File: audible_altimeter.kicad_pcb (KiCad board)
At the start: 2 copper layers, 43 parts, among them CON1 BUQ2-USB-MICRO-B, IC1 BUQ2-ATXMEGA128A4U-A, P1 CONN_2, Q1 NPN, U1 MCP7940M, U10 LINX-FM-GPS, U11 SI7020-A10, U2 MCP73831-SOT-23-5, U3 NCP4681-SC-70, U4 MICRO-SD-CONN, U5 MPL3115A2, U6 LS013B4DN04, U7 CSS-0575A-SMT, U8 TAG-CONNECT-ATMEL-PDI-CONNECT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, U9 MPU-9250, X1 CRYSTAL

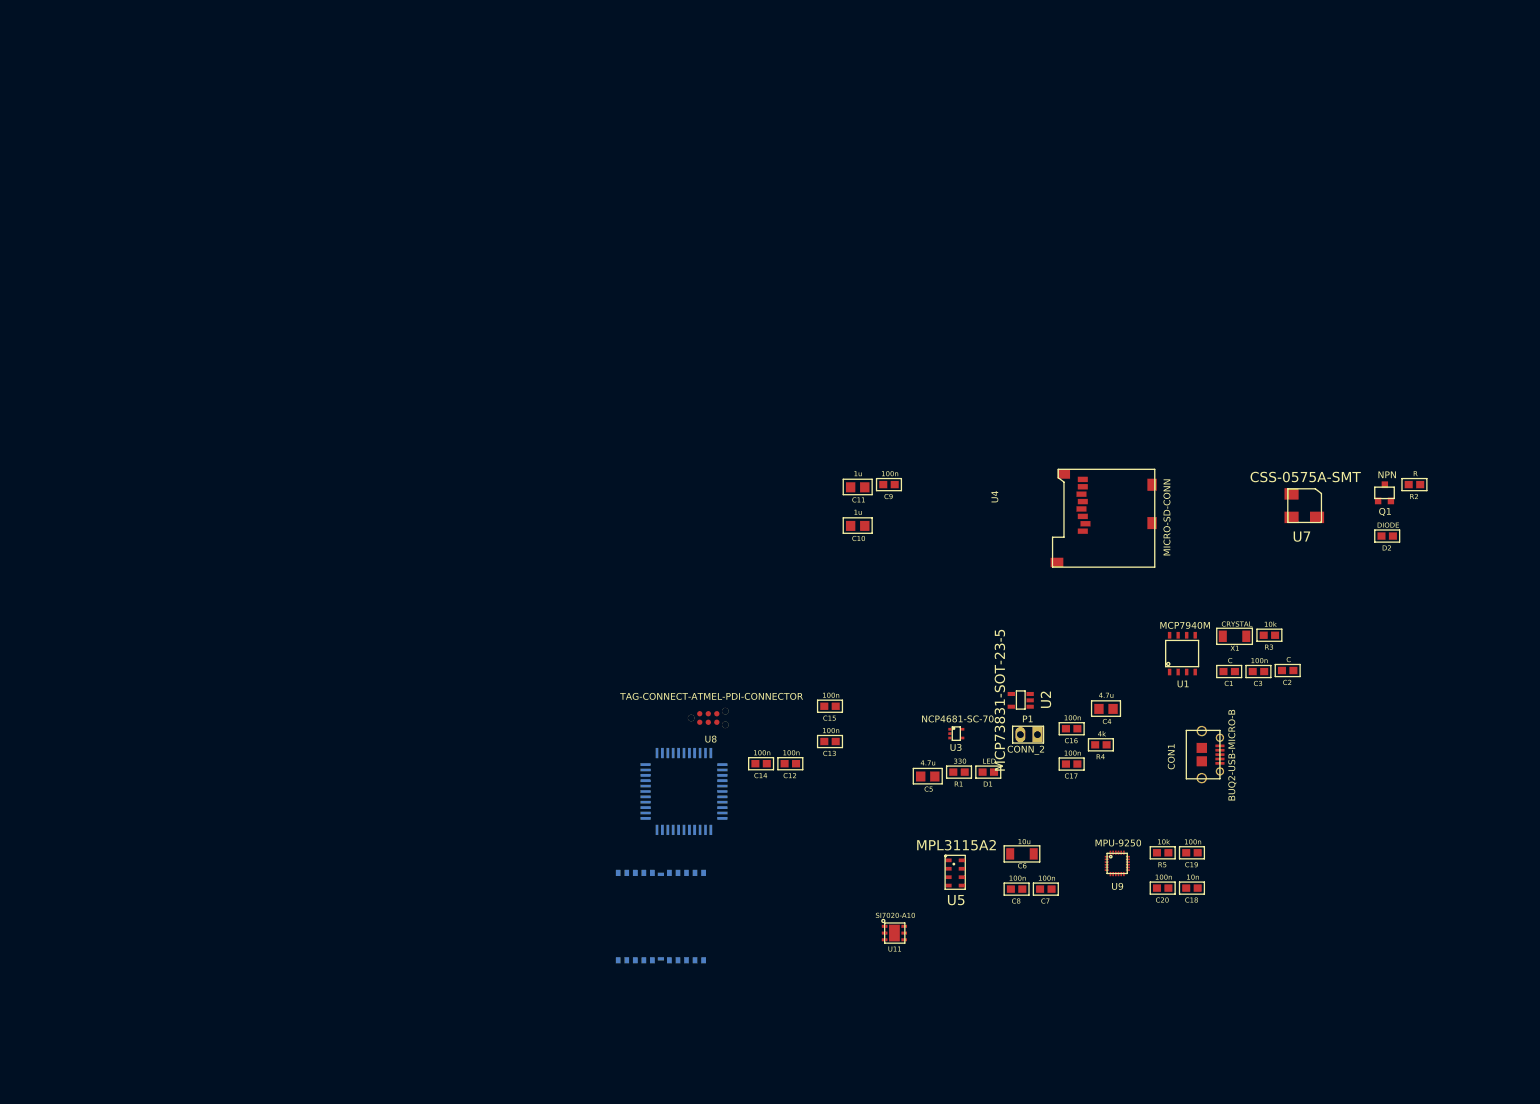
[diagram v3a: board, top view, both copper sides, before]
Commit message: Add buttons. Fix DRC. Add antenna
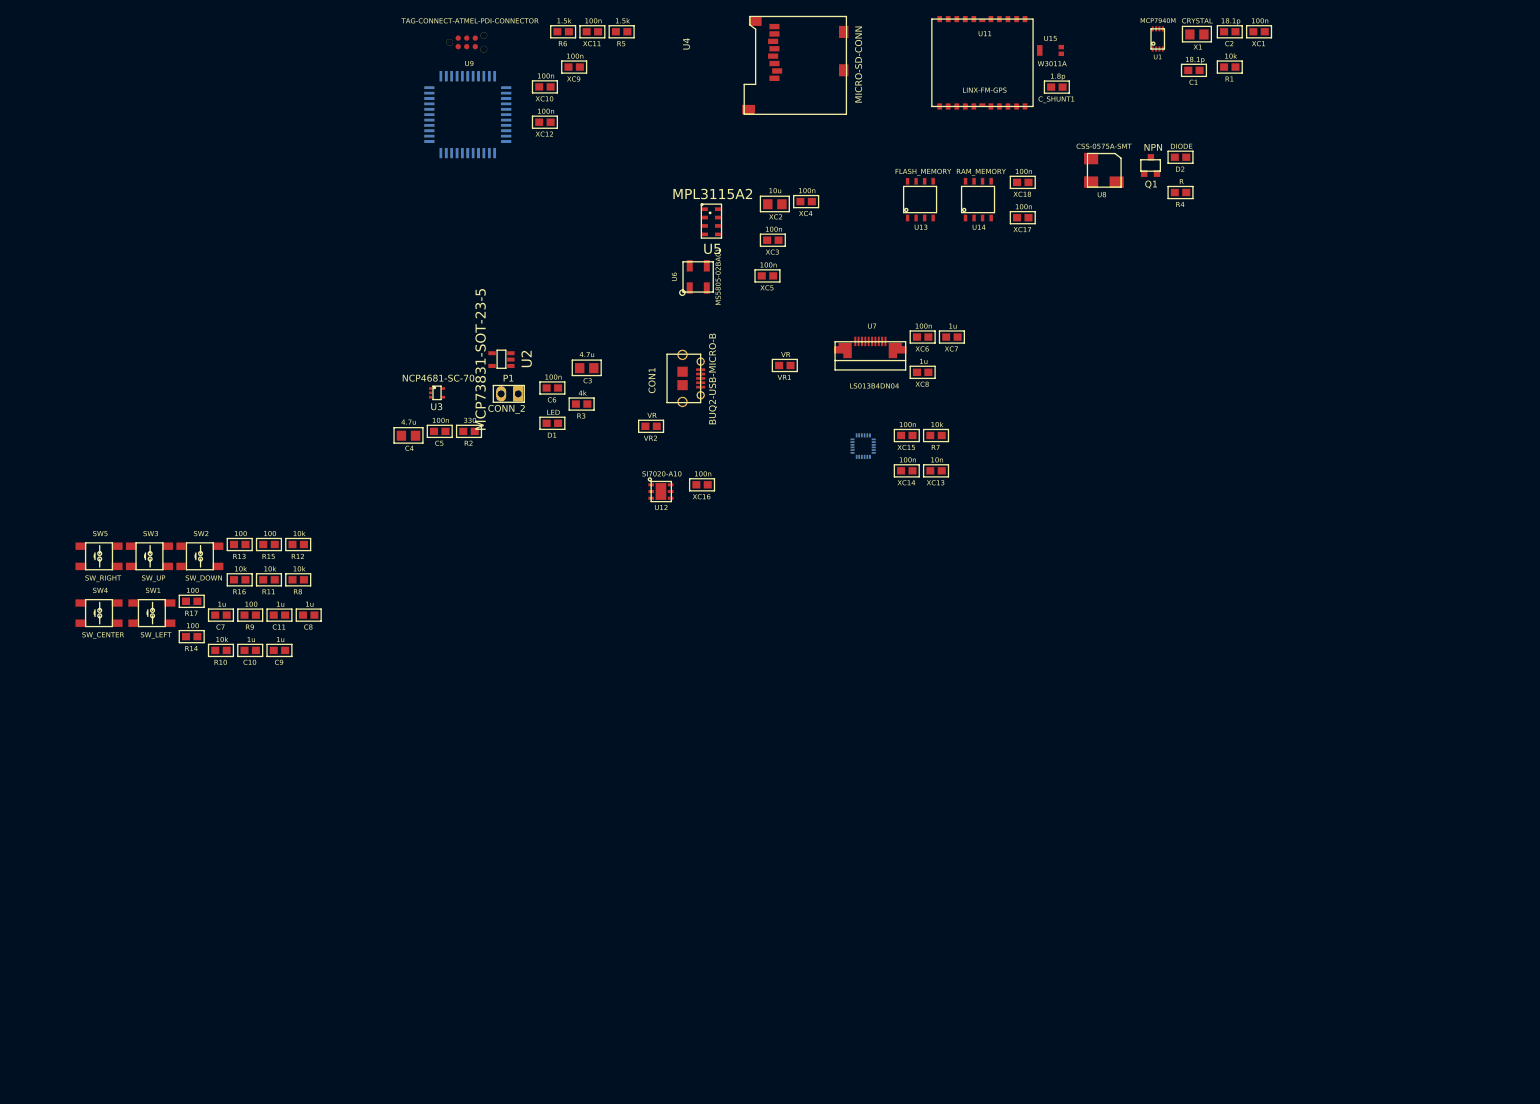
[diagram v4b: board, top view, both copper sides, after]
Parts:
- removed C12, C13, C14, C15, C16, C17, C19, C20: 100n, buq2:SM0603
- removed C18: 10n, buq2:SM0603
- added C_SHUNT1: 1.8p, buq2:SM0603, F.Cu at (202.6, -60.4)
- added LS013B4DN04-FPC: VAL**, buq2:LS013B4DN04-FPC, F.Cu at (150.2, 37.3)
- added R10: 10k, buq2:SM0603, F.Cu at (78.3, 23.4)
- added R11: 10k, buq2:SM0603, F.Cu at (85.4, 12.9)
- added R12: 10k, buq2:SM0603, F.Cu at (89.8, 7.61)
- added R13: 100, buq2:SM0603, F.Cu at (81.1, 7.61)
- added R14: 100, buq2:SM0603, F.Cu at (73.9, 21.3)
- added R15: 100, buq2:SM0603, F.Cu at (85.4, 7.61)
- added R16: 10k, buq2:SM0603, F.Cu at (81.1, 12.9)
- added R17: 100, buq2:SM0603, F.Cu at (73.9, 16.1)
- added R6: 1.5k, buq2:SM0603, F.Cu at (129.2, -68.6)
- added R7: 10k, buq2:SM0603, F.Cu at (184.6, -8.60)
- added R8: 10k, buq2:SM0603, F.Cu at (89.8, 12.9)
- added R9: 100, buq2:SM0603, F.Cu at (82.6, 18.1)
- added SW1: SW_LEFT, buq2:PUSHBUTTON_4x4_ROTATED, F.Cu at (68.0, 17.7)
- added SW2: SW_DOWN, buq2:PUSHBUTTON_4x4_ROTATED, F.Cu at (75.2, 9.26)
- added SW3: SW_UP, buq2:PUSHBUTTON_4x4_ROTATED, F.Cu at (67.7, 9.26)
- added SW4: SW_CENTER, buq2:PUSHBUTTON_4x4_ROTATED, F.Cu at (60.2, 17.7)
- added SW5: SW_RIGHT, buq2:PUSHBUTTON_4x4_ROTATED, F.Cu at (60.2, 9.26)
- added U12: SI7020-A10, buq2:DFN-6-3X3MM, F.Cu at (143.7, -0.27)
- added U13: FLASH_MEMORY, buq2:8-SOIC, F.Cu at (180.4, -40.9)
- added U14: RAM_MEMORY, buq2:8-SOIC, F.Cu at (189.0, -40.9)
- added U15: W3011A, buq2:W3011A, F.Cu at (201.7, -65.9)
- added VR1: VR, buq2:SM0603, F.Cu at (162.1, -19.0)
- added VR2: VR, buq2:SM0603, F.Cu at (142.3, -9.97)
- added XC1: 100n, buq2:SM0603, F.Cu at (232.7, -68.6)
- added XC10: 100n, buq2:SM0603, F.Cu at (126.5, -60.4)
- added XC11: 100n, buq2:SM0603, F.Cu at (133.5, -68.6)
- added XC12: 100n, buq2:SM0603, F.Cu at (126.5, -55.2)
- added XC13: 10n, buq2:SM0603, F.Cu at (184.6, -3.35)
- added XC14: 100n, buq2:SM0603, F.Cu at (180.3, -3.35)
- added XC15: 100n, buq2:SM0603, F.Cu at (180.3, -8.60)
- added XC16: 100n, buq2:SM0603, F.Cu at (149.8, -1.27)
- added XC17: 100n, buq2:SM0603, F.Cu at (197.5, -41.0)
- added XC18: 100n, buq2:SM0603, F.Cu at (197.5, -46.2)
- added XC2: 10u, buq2:SM0805, F.Cu at (160.7, -43.0)
- added XC3: 100n, buq2:SM0603, F.Cu at (160.4, -37.6)
- added XC4: 100n, buq2:SM0603, F.Cu at (165.3, -43.4)
- added XC5: 100n, buq2:SM0603, F.Cu at (159.6, -32.3)
- added XC6: 100n, buq2:SM0603, F.Cu at (182.6, -23.2)
- added XC7: 1u, buq2:SM0603, F.Cu at (187.0, -23.2)
- added XC8: 1u, buq2:SM0603, F.Cu at (182.6, -18.0)
- added XC9: 100n, buq2:SM0603, F.Cu at (130.8, -63.4)
- C1, C2: value C -> 18.1p
- C10, C11: footprint buq2:SM0805 -> buq2:SM0603
- C3: value 100n -> 4.7u; footprint buq2:SM0603 -> buq2:SM0805
- C5: value 4.7u -> 100n; footprint buq2:SM0805 -> buq2:SM0603
- C6: value 10u -> 100n; footprint buq2:SM1206 -> buq2:SM0603
- C7, C8, C9: value 100n -> 1u
- R1: value 330 -> 10k
- R2: value R -> 330
- R3: value 10k -> 4k
- R4: value 4k -> R
- R5: value 10k -> 1.5k
- U1: footprint buq2:8-SOIC -> buq2:8-TDFN
- U10: value LINX-FM-GPS -> MPU-9250; footprint buq2:LINX-FM-GPS -> buq2:24QFN-3MM-3MM
- U11: value SI7020-A10 -> LINX-FM-GPS; footprint buq2:DFN-6-3X3MM -> buq2:LINX-FM-GPS
- U6: value LS013B4DN04 -> MS5805-02BA01; footprint buq2:LS013B7DH03-FPC -> buq2:MS5805-02BA01
- U7: value CSS-0575A-SMT -> LS013B4DN04; footprint buq2:BUZZER-CUI-5MM -> buq2:FPC-CONN-10-FCI-BOTTOM-CONTACTS
- U8: value TAG-CONNECT-ATMEL-PDI-CONNECTOR -> CSS-0575A-SMT; footprint buq2:TAG-CONNECT6 -> buq2:BUZZER-CUI-5MM
- U9: value MPU-9250 -> TAG-CONNECT-ATMEL-PDI-CONNECTOR; footprint buq2:24QFN-3MM-3MM -> buq2:TAG-CONNECT6
- X1: footprint buq2:SM1206 -> buq2:SM0805
- moved U9 155.7 mm to (112.3, -67.1)
- moved R5 146.2 mm to (137.9, -68.6)
- moved R2 140.8 mm to (115.2, -9.22)
- moved U11 130.1 mm to (191.6, -64.0)
- moved C7 129.3 mm to (78.3, 18.1)
- moved C8 112.9 mm to (91.3, 18.1)
- moved R1 112.3 mm to (228.3, -63.4)
- moved C4 111.4 mm to (106.2, -8.57)
- moved C3 109.6 mm to (132.7, -18.6)
- moved R3 107.9 mm to (131.9, -13.3)
- moved IC1 105.7 mm to (115.0, -56.3)
- moved U5 103.4 mm to (151.2, -40.4)
- moved U8 99.4 mm to (207.7, -46.3)
- moved C6 98.4 mm to (127.6, -15.7)
- moved C2 95.4 mm to (228.3, -68.6)
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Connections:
- C10 pad 1: /Display/VDD -> Net-(C10-Pad1)
- C11 pad 1: /Display/VDD -> Net-(C11-Pad1)
- C11 pad 2: (no net) -> GND
- C3 pad 1: GND -> /Battery/BATTERY
- C3 pad 2: /Clock/VCC -> GND
- C4 pad 1: /Battery/BATTERY -> /Battery/+5V
- C5 pad 1: /Battery/+5V -> GND
- C5 pad 2: GND -> /Battery/+5V
- C6 pad 1: GND -> /Battery/+3.3V
- C6 pad 2: /Barometer/VCC -> GND
- C7 pad 1: GND -> Net-(C7-Pad1)
- C7 pad 2: /Barometer/VCC -> GND
- C9 pad 1: (no net) -> Net-(C9-Pad1)
- CON1 pad 1: (no net) -> /Battery/+5V
- CON1 pad 2: (no net) -> /MCU/D-
- CON1 pad 3: (no net) -> /MCU/D+
- D2 pad 2: /Buzzer/BATTERY -> /Battery/BATTERY
- IC1 pad 1: (no net) -> /Buttons/BUTTON_UP
- IC1 pad 10: (no net) -> /9-Axis/I2C_SDA
- IC1 pad 11: (no net) -> /9-Axis/I2C_SCL
- IC1 pad 15: (no net) -> /Display/MOSI
- IC1 pad 16: (no net) -> /MCU/MISO
- IC1 pad 17: (no net) -> /MCU/SCK
- IC1 pad 19: MCU_VCC -> /Battery/+3.3V
- IC1 pad 2: (no net) -> /Buttons/BUTTON_DOWN
- IC1 pad 20: (no net) -> /MCU/CSn_FLASH
- IC1 pad 21: (no net) -> /MCU/CSn_RAM
- IC1 pad 22: (no net) -> /Display/CS
- IC1 pad 23: (no net) -> /MicroSD/CSn
- IC1 pad 26: (no net) -> /MCU/D-
- IC1 pad 27: (no net) -> /MCU/D+
- IC1 pad 3: (no net) -> /Buttons/BUTTON_LEFT
- IC1 pad 31: MCU_VCC -> /Battery/+3.3V
- IC1 pad 32: (no net) -> /GPS/RX
- IC1 pad 33: (no net) -> /GPS/TX
- IC1 pad 34: PDI_DATA -> /MCU/PDI_DATA
- IC1 pad 35: PDI_CLK -> /MCU/PDI_CLK
- IC1 pad 39: MCU_VCC -> /Battery/+3.3V
- IC1 pad 4: (no net) -> /Buttons/BUTTON_RIGHT
- IC1 pad 40: (no net) -> /MCU/CLOCK_INT
- IC1 pad 41: (no net) -> /MCU/ACCELERATOR_INT
- IC1 pad 42: (no net) -> /MCU/BAROMETER_INT
- IC1 pad 43: (no net) -> /MicroSD/CARD_DETECT
- IC1 pad 44: (no net) -> /MCU/GPS_PULSE_PER_SECOND
- IC1 pad 5: (no net) -> /Buttons/BUTTON_CENTER
- IC1 pad 6: (no net) -> /MCU/DISPLAY_INVERT
- IC1 pad 7: (no net) -> /Buzzer/BUZZER_DRIVE
- IC1 pad 9: MCU_VCC -> /Battery/+3.3V
- R1 pad 1: Net-(D1-Pad2) -> /Battery/+3.3V
- R1 pad 2: Net-(R1-Pad2) -> /MCU/CLOCK_INT
- R2 pad 1: Net-(Q1-Pad2) -> Net-(D1-Pad2)
- R2 pad 2: (no net) -> Net-(R2-Pad2)
- R3 pad 1: /Clock/VCC -> Net-(R3-Pad1)
- R3 pad 2: /Clock/MULTI_FUNCTIONAL -> GND
- R4 pad 1: Net-(R4-Pad1) -> Net-(Q1-Pad2)
- R4 pad 2: GND -> /Buzzer/BUZZER_DRIVE
- R5 pad 1: GND -> /Battery/+3.3V
- R5 pad 2: /9-Axis/INT -> /9-Axis/I2C_SCL
- U1 pad 5: (no net) -> /9-Axis/I2C_SDA
- U1 pad 6: (no net) -> /9-Axis/I2C_SCL
- U1 pad 7: /Clock/MULTI_FUNCTIONAL -> /MCU/CLOCK_INT
- U1 pad 8: /Clock/VCC -> /Battery/+3.3V
- U10 pad 1: (no net) -> /Battery/+3.3V
- U10 pad 10: (no net) -> Net-(U10-Pad10)
- U10 pad 11: /GPS/VCC -> GND
- U10 pad 12: /GPS/VCC -> /MCU/ACCELERATOR_INT
- U10 pad 13: (no net) -> /Battery/+3.3V
- U10 pad 21: GND -> (no net)
- U10 pad 22: GND -> /Battery/+3.3V
- U10 pad 8: (no net) -> /Battery/+3.3V
- U10 pad 9: (no net) -> GND
- U11 pad 2: GND -> (no net)
- U11 pad 3: (no net) -> /MCU/GPS_PULSE_PER_SECOND
- U11 pad 4: (no net) -> /GPS/TX
- U11 pad 5: (no net) -> /GPS/RX
- U2 pad 1: Net-(R1-Pad2) -> Net-(R2-Pad2)
- U2 pad 5: Net-(R4-Pad1) -> Net-(R3-Pad1)
- U4 pad 2: (no net) -> /MicroSD/CSn
- U4 pad 3: (no net) -> /Display/MOSI
- U4 pad 4: (no net) -> /Battery/+3.3V
- U4 pad 5: (no net) -> /MCU/SCK
- U4 pad 7: (no net) -> /MCU/MISO
- U4 pad 9: (no net) -> /MicroSD/CARD_DETECT
- U5 pad 1: /Barometer/VCC -> /Battery/+3.3V
- U5 pad 2: Net-(C8-Pad1) -> Net-(U5-Pad2)
- U5 pad 4: /Barometer/VCC -> /Battery/+3.3V
- U5 pad 6: (no net) -> /MCU/BAROMETER_INT
- U5 pad 7: (no net) -> /9-Axis/I2C_SDA
- U5 pad 8: (no net) -> /9-Axis/I2C_SCL
- U7 pad 1: /Buzzer/BATTERY -> /MCU/SCK
- U7 pad 2: Net-(D2-Pad1) -> /Display/MOSI
- U7 pad 3: (no net) -> /Display/CS
- U8 pad 1: PDI_DATA -> /Battery/BATTERY
- U8 pad 2: MCU_VCC -> Net-(D2-Pad1)
- U9 pad 1: /9-Axis/VDD -> /MCU/PDI_DATA
- U9 pad 2: (no net) -> /Battery/+3.3V
- U9 pad 5: (no net) -> /MCU/PDI_CLK
- U9 pad 6: (no net) -> GND

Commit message: Start first layout test
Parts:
- C10, C11, C7, C9, R11, R12, R14, R15, R16, R17, R8, R9, U4, U7, XC6, XC7, XC8: moved to B.Cu
- moved U15 151.6 mm to (104.5, 50.5)
- moved C_SHUNT1 143.4 mm to (110.1, 49.2), turned to 90 degrees
- moved XC6 131.8 mm to (64.2, 34.6)
- moved XC7 131.8 mm to (68.6, 34.6)
- moved XC8 131.8 mm to (64.2, 39.8)
- moved U11 128.8 mm to (120.3, 43.2), turned to 270 degrees
- moved D2 124.8 mm to (175.5, 66.2)
- moved Q1 124.8 mm to (171.1, 67.4)
- moved R4 124.8 mm to (175.5, 71.5)
- moved U8 117.9 mm to (137.9, 48.7)
- moved U4 105.1 mm to (136.5, 35.6), turned to 0 degrees
- moved IC1 93.2 mm to (124.1, 36.4)
- moved SW5 92.2 mm to (149.1, 33.5), turned to 270 degrees
- moved U7 85.3 mm to (113.9, 39.3), turned to 90 degrees
- moved SW4 84.4 mm to (143.1, 33.5), turned to 90 degrees
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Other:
- board outline added: 52.4 x 29.3 mm

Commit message: Little bit layout
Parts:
- C10, C11, C7, C9, R11, R12, R14, R15, R16, R17, R8, R9, U10, U4: moved to F.Cu
- R5, R6, XC10, XC11, XC12, XC9: moved to B.Cu
- moved C4 163.8 mm to (265.7, 28.7)
- moved R2 151.6 mm to (260.5, 34.0)
- moved C5 146.9 mm to (251.0, 34.8)
- moved R6 144.4 mm to (229.2, 35.4), turned to 270 degrees
- moved D1 144.3 mm to (264.8, 34.0)
- moved U9 144.0 mm to (220.4, 28.2), turned to 90 degrees
- moved XC9 143.4 mm to (234.3, 35.9), turned to 180 degrees
- moved XC12 143.2 mm to (238.6, 33.9)
- moved XC1 141.0 mm to (230.8, 72.4), turned to 90 degrees
- moved X1 140.0 mm to (243.0, 70.4)
- moved XC11 138.6 mm to (229.7, 31.1), turned to 90 degrees
- moved C2 138.5 mm to (237.6, 69.6), turned to 90 degrees
- moved R5 138.5 mm to (236.2, 28.9), turned to 270 degrees
- moved C3 136.6 mm to (260.8, 28.7)
- moved XC10 135.6 mm to (232.2, 24.5), turned to 270 degrees
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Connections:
- IC1 pad 2: /Buttons/BUTTON_DOWN -> /Buttons/BUTTON_LEFT
- IC1 pad 3: /Buttons/BUTTON_LEFT -> /Buttons/BUTTON_CENTER
- IC1 pad 5: /Buttons/BUTTON_CENTER -> /Buttons/BUTTON_DOWN
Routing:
- net GND: track 0.00 -> 192.7 mm
- net /Battery/+3.3V: track 0.00 -> 45.9 mm
- net Net-(C9-Pad1): track 0.00 -> 32.5 mm
- net /Battery/BATTERY: track 0.00 -> 32.1 mm, vias 0 -> 2
- net Net-(C11-Pad1): track 0.00 -> 31.5 mm, vias 0 -> 4
- net Net-(C10-Pad1): track 0.00 -> 24.1 mm
- net Net-(C7-Pad1): track 0.00 -> 22.6 mm
- net Net-(C8-Pad1): track 0.00 -> 21.5 mm
- net /Battery/+5V: track 0.00 -> 13.7 mm
- net Net-(C_SHUNT1-Pad2): track 0.00 -> 11.4 mm
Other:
- net class Default: clearance 0.254 -> 0.1524; trace_width 0.254 -> 0.1524; via_dia 0.889 -> 0.6858; via_drill 0.635 -> 0.3302
- rule trace_clearance: 0.254 -> 0.1524
- rule trace_min: 0.254 -> 0.1524
- rule via_min_drill: 0.508 -> 0.3302
- rule via_min_size: 0.889 -> 0.6858

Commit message: Some easy routing
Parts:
- moved IC1 2.00 mm to (124.8, 35.5)
- moved R13 0.40 mm to (134.8, 38.5)
- moved R14 0.40 mm to (134.8, 30.5)
- moved R15 0.40 mm to (134.8, 34.5)
- moved R17 0.40 mm to (134.8, 36.5)
- moved R9 0.40 mm to (134.8, 32.5)
- moved SW3 0.38 mm to (143.7, 28.8)
- moved SW2 0.38 mm to (143.7, 41.4)
- moved SW1 0.25 mm to (139.0, 35.0)
- moved SW4 0.16 mm to (143.6, 35.0)
- moved SW5 0.09 mm to (148.4, 35.0)
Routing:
- net /Battery/+3.3V: track 45.9 -> 75.1 mm
- net GND: track 192.7 -> 210.9 mm
- net /GPS/TX: track 0.00 -> 10.5 mm, vias 0 -> 1
- net /GPS/RX: track 0.00 -> 8.82 mm, vias 0 -> 1
- net Net-(C8-Pad1): track 21.5 -> 28.6 mm
- net /Buttons/BUTTON_DOWN: track 0.00 -> 6.30 mm, vias 0 -> 1
- net /Buttons/BUTTON_RIGHT: track 0.00 -> 4.64 mm, vias 0 -> 1
- net /Buttons/BUTTON_CENTER: track 0.00 -> 4.02 mm, vias 0 -> 1
- net /Buttons/BUTTON_UP: track 0.00 -> 3.85 mm, vias 0 -> 1
- net /Buttons/BUTTON_LEFT: track 0.00 -> 3.52 mm, vias 0 -> 1
- net Net-(C9-Pad1): track 32.5 -> 33.1 mm
- net Net-(C10-Pad1): track 24.1 -> 24.6 mm

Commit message: Layouting
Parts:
- U4: moved to B.Cu
- moved C4 156.9 mm to (108.8, 28.8), turned to 180 degrees
- moved C3 155.4 mm to (105.3, 26.9), turned to 90 degrees
- moved R2 154.8 mm to (106.0, 23.9)
- moved D1 152.5 mm to (112.6, 24.6), turned to 90 degrees
- moved R3 145.9 mm to (109.8, 23.9), turned to 180 degrees
- moved C5 135.1 mm to (116.0, 28.0), turned to 90 degrees
- moved XC15 134.5 mm to (137.4, 46.7), turned to 0 degrees
- moved C6 133.7 mm to (113.1, 29.1), turned to 180 degrees
- moved R7 133.5 mm to (138.4, 49.7), turned to 90 degrees
- moved XC13 133.2 mm to (133.2, 50.6), turned to 0 degrees
- moved D2 129.6 mm to (117.7, 46.0), turned to 180 degrees
- moved XC14 129.4 mm to (136.6, 49.7)
- moved R4 128.0 mm to (120.2, 48.7), turned to 90 degrees
- moved Q1 125.4 mm to (117.3, 48.5)
- moved U10 125.1 mm to (131.8, 46.4)
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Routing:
- net /Battery/+3.3V: track 75.1 -> 147.4 mm, vias 0 -> 2
- net GND: track 210.9 -> 265.7 mm
- net /MCU/PDI_CLK: track 0.00 -> 22.2 mm, vias 0 -> 1
- net /MCU/PDI_DATA: track 0.00 -> 17.8 mm, vias 0 -> 1
- net /Buzzer/BUZZER_DRIVE: track 0.00 -> 17.6 mm, vias 0 -> 3
- net /MCU/ACCELERATOR_INT: track 0.00 -> 14.0 mm, vias 0 -> 2
- net /MCU/D-: track 0.00 -> 12.2 mm, vias 0 -> 1
- net /MCU/D+: track 0.00 -> 10.9 mm, vias 0 -> 1
- net Net-(D2-Pad1): track 0.00 -> 10.4 mm
- net Net-(D1-Pad2): track 0.00 -> 8.23 mm
- net /9-Axis/I2C_SCL: track 0.00 -> 7.61 mm, vias 0 -> 4
- net /9-Axis/I2C_SDA: track 0.00 -> 7.19 mm, vias 0 -> 4
- net Net-(C2-Pad1): track 0.00 -> 5.79 mm
- net Net-(C1-Pad1): track 0.00 -> 4.52 mm
- net /Battery/+5V: track 13.7 -> 17.8 mm
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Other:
- outline, holes or cut-outs redrawn
